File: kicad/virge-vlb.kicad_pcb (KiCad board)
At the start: 4 copper layers, 240.5 x 69.4 mm, 97 parts, among them CN1 VGA, J1 VLB_slot, U1 74LS245, U2 27C020, U3 V53C16258H, U4 V53C16258H, U5 V53C16258H, U6 V53C16258H, U7 86C325, U8 7404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

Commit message: updated VLB footprint
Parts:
- U7: value 86C325 -> 86C765
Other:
- outline, holes or cut-outs redrawn

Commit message: fixed VGA footprint
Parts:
- moved CN1 1.11 mm to (259.4, 99.8)
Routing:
- net GND: track 162.6 -> 155.6 mm
- net /BLUE: track 24.7 -> 23.6 mm
- net /RED: track 14.4 -> 13.2 mm
- net /GREEN: track 19.5 -> 18.3 mm

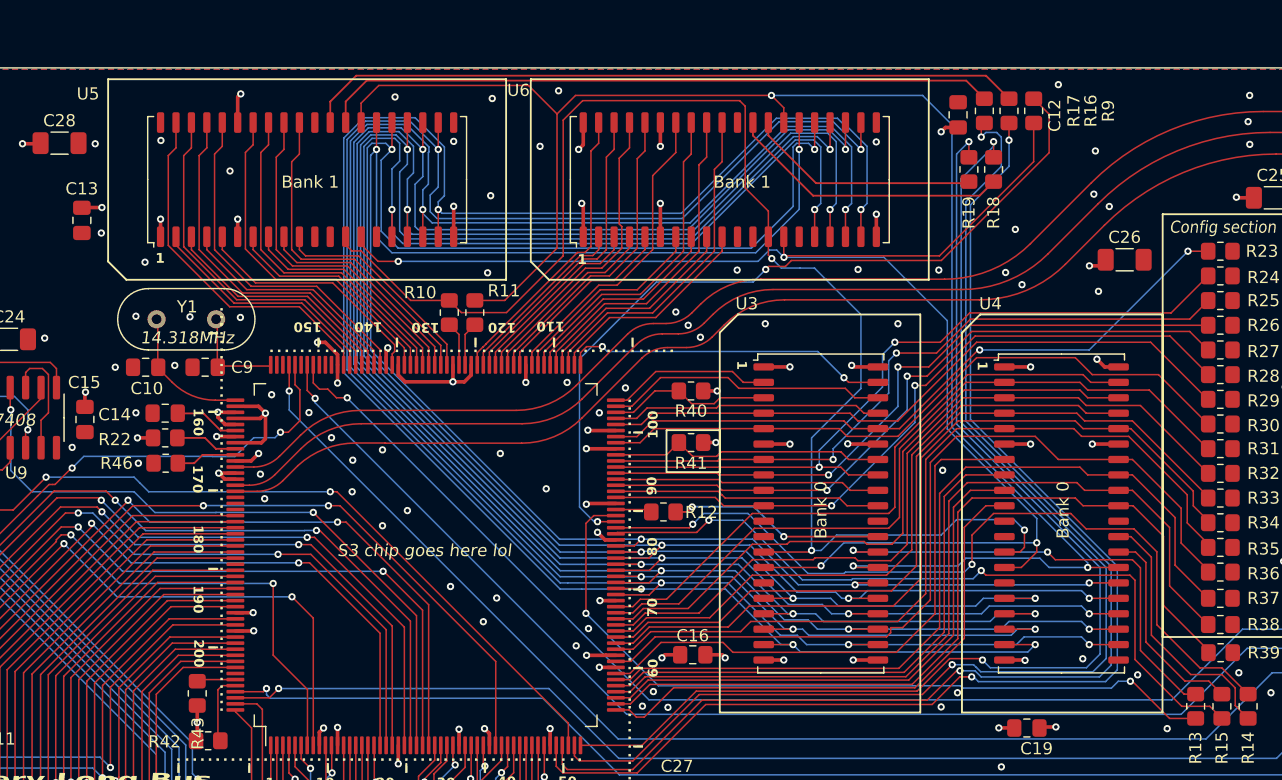
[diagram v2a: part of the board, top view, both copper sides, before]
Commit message: enlarged SOJ pads
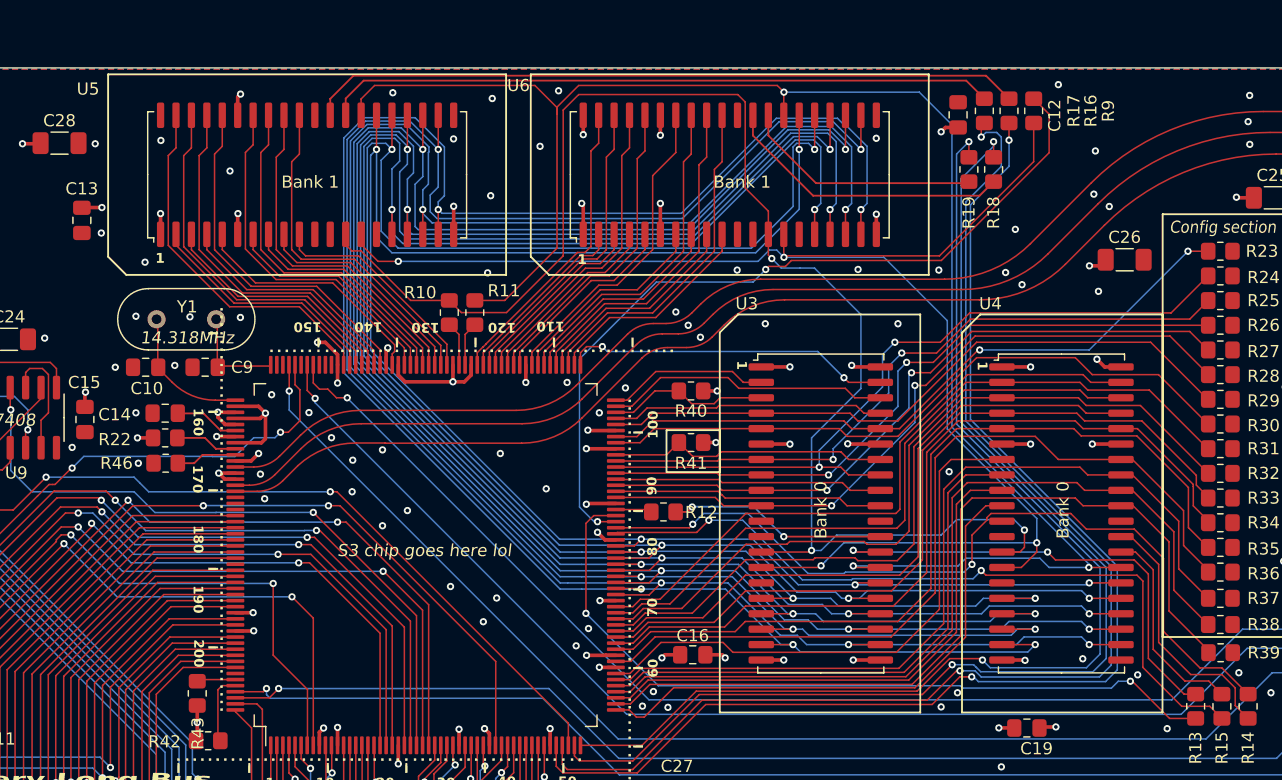
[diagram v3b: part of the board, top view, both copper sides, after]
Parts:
- moved U5 0.40 mm to (68.3, 84.3)
- moved U6 0.40 mm to (103.1, 84.3)
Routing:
- net GND: track 155.6 -> 153.3 mm
- net /Memory Bus/OE: track 141.3 -> 142.7 mm
- net /Memory Bus/WE: track 119.8 -> 120.9 mm
- net VCC: track 143.3 -> 144.2 mm
- net /Memory Bus/PD29: track 53.9 -> 54.6 mm
